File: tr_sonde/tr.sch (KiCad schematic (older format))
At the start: 90 parts, among them J1 SMA, J2 SMA, J3 SMA, K1 SMDHDR, K2 SMDHDR, K3 SMDHDR, Q1 PBSS4250X, Q2 MMBT2222A, Q3 STD2NK90ZT4, Q4 STD2NK90ZT4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

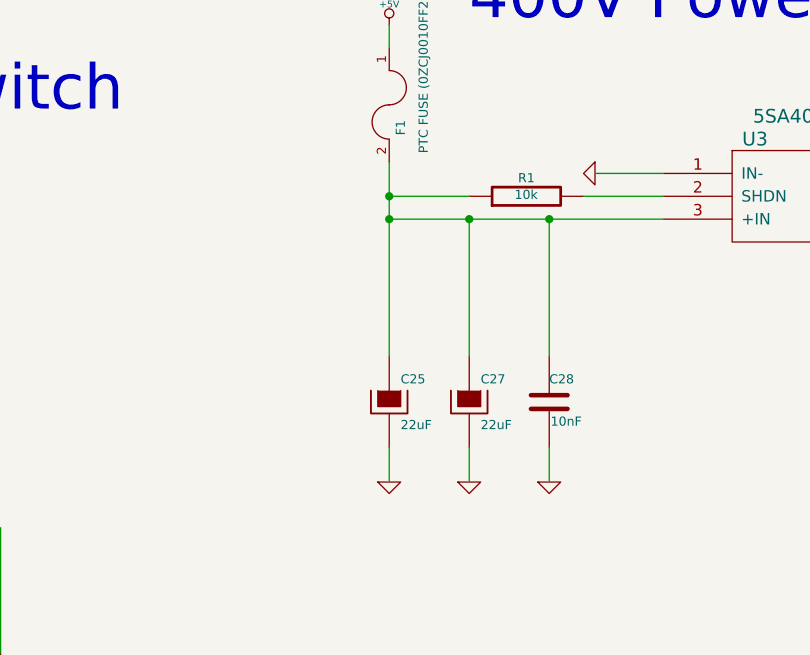
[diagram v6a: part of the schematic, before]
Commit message: component footprint changes to simplify bom
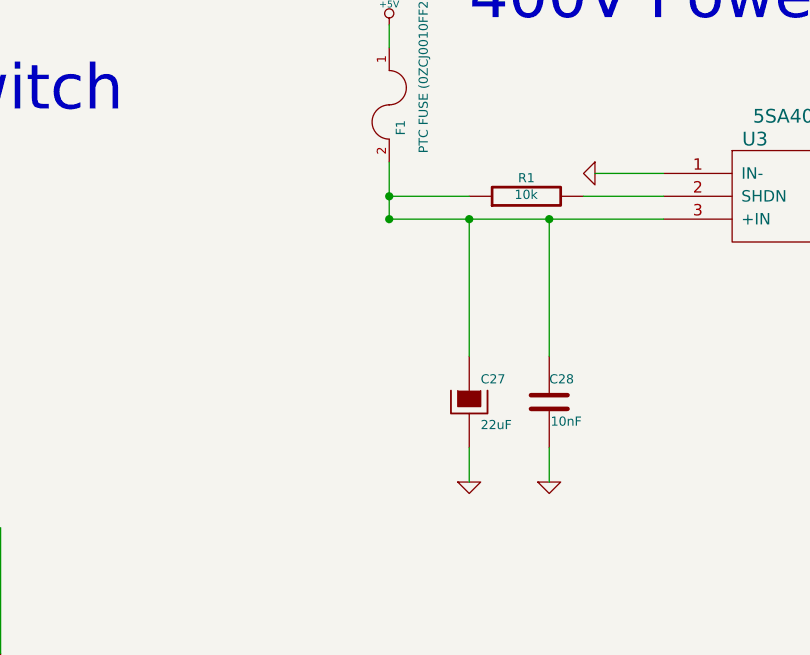
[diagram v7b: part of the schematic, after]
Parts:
- removed C25: 22uF, smd_capacitors:c_1210, symbol CAPAPOL
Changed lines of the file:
@@
-	1    0    0    -1
-$EndComp
-$Comp
-L CAPAPOL C25
-U 1 1 52E6B8A9
-P 8400 2550
-F 0 "C25" H 8450 2650 40  0000 L CNN
-F 1 "22uF" H 8450 2450 40  0000 L CNN
-F 2 "smd_capacitors:c_1210" H 8500 2400 30  0001 C CNN
-F 3 "~" H 8400 2550 300 0000 C CNN
-F 4 "GRM32ER61C476ME15L" H 8400 2550 60  0001 C CNN "DIGIKEYPN"
-	1    8400 2550
-	1    0    0    -1
-$EndComp
-$Comp
-L GND #PWR027
-U 1 1 52E6B8AF
-P 8400 2900
-F 0 "#PWR027" H 8400 2900 30  0001 C CNN
-F 1 "GND" H 8400 2830 30  0001 C CNN
-F 2 "" H 8400 2900 60  0000 C CNN
-F 3 "" H 8400 2900 60  0000 C CNN
-	1    8400 2900
 	1    0    0    -1
 $EndComp
@@
 $EndComp
 $Comp
-L GND #PWR028
+L GND #PWR027
 U 1 1 53376FDF
 P 13900 3550
-F 0 "#PWR028" H 13900 3550 30  0001 C CNN
+F 0 "#PWR027" H 13900 3550 30  0001 C CNN
 F 1 "GND" H 13900 3480 30  0001 C CNN
 F 2 "" H 13900 3550 60  0000 C CNN
@@
 $EndComp
 $Comp
-L VCC #PWR029
+L VCC #PWR028
 U 1 1 5337703B
 P 12750 2900
-F 0 "#PWR029" H 12750 3000 30  0001 C CNN
+F 0 "#PWR028" H 12750 3000 30  0001 C CNN
 F 1 "VCC" H 12750 3000 30  0000 C CNN
 F 2 "" H 12750 2900 60  0000 C CNN
@@
 $EndComp
 $Comp
-L GND #PWR030
+L GND #PWR029
 U 1 1 53484265
 P 11350 2500
-F 0 "#PWR030" H 11350 2500 30  0001 C CNN
+F 0 "#PWR029" H 11350 2500 30  0001 C CNN
 F 1 "GND" H 11350 2430 30  0001 C CNN
 F 2 "" H 11350 2500 60  0000 C CNN
@@
 $EndComp
 $Comp
-L GND #PWR031
+L GND #PWR030
 U 1 1 534843BD
 P 11700 2500
-F 0 "#PWR031" H 11700 2500 30  0001 C CNN
+F 0 "#PWR030" H 11700 2500 30  0001 C CNN
 F 1 "GND" H 11700 2430 30  0001 C CNN
 F 2 "" H 11700 2500 60  0000 C CNN
@@
 $EndComp
 $Comp
-L GND #PWR032
+L GND #PWR031
 U 1 1 534C743A
 P 4950 3400
-F 0 "#PWR032" H 4950 3400 30  0001 C CNN
+F 0 "#PWR031" H 4950 3400 30  0001 C CNN
 F 1 "GND" H 4950 3330 30  0001 C CNN
 F 2 "" H 4950 3400 60  0000 C CNN
@@
 $EndComp
 $Comp
-L +5V #PWR033
+L +5V #PWR032
 U 1 1 537E540A
 P 10900 7350
-F 0 "#PWR033" H 10900 7440 20  0001 C CNN
+F 0 "#PWR032" H 10900 7440 20  0001 C CNN
 F 1 "+5V" H 10900 7440 30  0000 C CNN
 F 2 "" H 10900 7350 60  0000 C CNN
@@
 $EndComp
 $Comp
-L GND #PWR034
+L GND #PWR033
 U 1 1 537E5711
 P 11100 8100
-F 0 "#PWR034" H 11100 8100 30  0001 C CNN
+F 0 "#PWR033" H 11100 8100 30  0001 C CNN
 F 1 "GND" H 11100 8030 30  0001 C CNN
 F 2 "" H 11100 8100 60  0000 C CNN
@@
 $EndComp
 $Comp
-L GND #PWR035
+L GND #PWR034
 U 1 1 537E5906
 P 9700 8650
-F 0 "#PWR035" H 9700 8650 30  0001 C CNN
+F 0 "#PWR034" H 9700 8650 30  0001 C CNN
 F 1 "GND" H 9700 8580 30  0001 C CNN
 F 2 "" H 9700 8650 60  0000 C CNN
@@
 $EndComp
 $Comp
-L +5V #PWR036
+L +5V #PWR035
 U 1 1 537E5D07
 P 15700 5400
-F 0 "#PWR036" H 15700 5490 20  0001 C CNN
+F 0 "#PWR035" H 15700 5490 20  0001 C CNN
 F 1 "+5V" H 15700 5490 30  0000 C CNN
 F 2 "" H 15700 5400 60  0000 C CNN
@@
 $EndComp
 $Comp
-L GND #PWR037
+L GND #PWR036
 U 1 1 537E7018
 P 12400 5600
-F 0 "#PWR037" H 12400 5600 30  0001 C CNN
+F 0 "#PWR036" H 12400 5600 30  0001 C CNN
 F 1 "GND" H 12400 5530 30  0001 C CNN
 F 2 "" H 12400 5600 60  0000 C CNN
@@
 $EndComp
 $Comp
-L GND #PWR038
+L GND #PWR037
 U 1 1 537E737F
 P 12100 5600
-F 0 "#PWR038" H 12100 5600 30  0001 C CNN
+F 0 "#PWR037" H 12100 5600 30  0001 C CNN
 F 1 "GND" H 12100 5530 30  0001 C CNN
 F 2 "" H 12100 5600 60  0000 C CNN
@@
 $EndComp
 $Comp
-L GND #PWR039
+L GND #PWR038
 U 1 1 537E74F6
 P 9300 1550
-F 0 "#PWR039" H 9300 1550 30  0001 C CNN
+F 0 "#PWR038" H 9300 1550 30  0001 C CNN
 F 1 "GND" H 9300 1480 30  0001 C CNN
 F 2 "" H 9300 1550 60  0000 C CNN
@@
 $EndComp
 $Comp
-L GND #PWR040
+L GND #PWR039
 U 1 1 537E78FB
 P 9100 2900
-F 0 "#PWR040" H 9100 2900 30  0001 C CNN
+F 0 "#PWR039" H 9100 2900 30  0001 C CNN
 F 1 "GND" H 9100 2830 30  0001 C CNN
 F 2 "" H 9100 2900 60  0000 C CNN
@@
 $EndComp
 $Comp
-L GND #PWR041
+L GND #PWR040
 U 1 1 537E7FEF
 P 10950 1550
-F 0 "#PWR041" H 10950 1550 30  0001 C CNN
+F 0 "#PWR040" H 10950 1550 30  0001 C CNN
 F 1 "GND" H 10950 1480 30  0001 C CNN
 F 2 "" H 10950 1550 60  0000 C CNN
@@
 $EndComp
 $Comp
-L GND #PWR042
+L GND #PWR041
 U 1 1 537E9221
 P 13500 2550
-F 0 "#PWR042" H 13500 2550 30  0001 C CNN
+F 0 "#PWR041" H 13500 2550 30  0001 C CNN
 F 1 "GND" H 13500 2480 30  0001 C CNN
 F 2 "" H 13500 2550 60  0000 C CNN
@@
 $EndComp
 $Comp
-L VCC #PWR043
+L VCC #PWR042
 U 1 1 537F9103
 P 9200 7600
-F 0 "#PWR043" H 9200 7700 30  0001 C CNN
+F 0 "#PWR042" H 9200 7700 30  0001 C CNN
 F 1 "VCC" H 9200 7700 30  0000 C CNN
 F 2 "" H 9200 7600 60  0000 C CNN
@@
 $EndComp
 $Comp
-L VCC #PWR044
+L VCC #PWR043
 U 1 1 537F913B
 P 11200 9450
-F 0 "#PWR044" H 11200 9550 30  0001 C CNN
+F 0 "#PWR043" H 11200 9550 30  0001 C CNN
 F 1 "VCC" H 11200 9550 30  0000 C CNN
 F 2 "" H 11200 9450 60  0000 C CNN
@@
 $EndComp
 $Comp
-L VDD #PWR045
+L VDD #PWR044
 U 1 1 537FA30C
 P 15550 750
-F 0 "#PWR045" H 15550 850 30  0001 C CNN
+F 0 "#PWR044" H 15550 850 30  0001 C CNN
 F 1 "VDD" H 15550 860 30  0000 C CNN
 F 2 "" H 15550 750 60  0000 C CNN
@@
 $EndComp
 $Comp
-L GND #PWR046
+L GND #PWR045
 U 1 1 537FA865
 P 15550 2950
-F 0 "#PWR046" H 15550 2950 30  0001 C CNN
+F 0 "#PWR045" H 15550 2950 30  0001 C CNN
 F 1 "GND" H 15550 2880 30  0001 C CNN
 F 2 "" H 15550 2950 60  0000 C CNN
@@
 $EndComp
 $Comp
-L GND #PWR047
+L GND #PWR046
 U 1 1 537FAD00
 P 15950 2950
-F 0 "#PWR047" H 15950 2950 30  0001 C CNN
+F 0 "#PWR046" H 15950 2950 30  0001 C CNN
 F 1 "GND" H 15950 2880 30  0001 C CNN
 F 2 "" H 15950 2950 60  0000 C CNN
@@
 $EndComp
 $Comp
-L VCC #PWR048
+L VCC #PWR047
 U 1 1 537FAE62
 P 14200 6300
-F 0 "#PWR048" H 14200 6400 30  0001 C CNN
+F 0 "#PWR047" H 14200 6400 30  0001 C CNN
 F 1 "VCC" H 14200 6400 30  0000 C CNN
 F 2 "" H 14200 6300 60  0000 C CNN
@@
 $EndComp
 $Comp
-L GND #PWR049
+L GND #PWR048
 U 1 1 537FB0A2
 P 14200 7800
-F 0 "#PWR049" H 14200 7800 30  0001 C CNN
+F 0 "#PWR048" H 14200 7800 30  0001 C CNN
 F 1 "GND" H 14200 7730 30  0001 C CNN
 F 2 "" H 14200 7800 60  0000 C CNN
@@
 $EndComp
 $Comp
-L GND #PWR050
+L GND #PWR049
 U 1 1 537FB41D
 P 14550 7800
-F 0 "#PWR050" H 14550 7800 30  0001 C CNN
+F 0 "#PWR049" H 14550 7800 30  0001 C CNN
 F 1 "GND" H 14550 7730 30  0001 C CNN
 F 2 "" H 14550 7800 60  0000 C CNN
@@
 $EndComp
 $Comp
-L GND #PWR051
+L GND #PWR050
 U 1 1 537FBBB2
 P 2900 4800
-F 0 "#PWR051" H 2900 4800 30  0001 C CNN
+F 0 "#PWR050" H 2900 4800 30  0001 C CNN
 F 1 "GND" H 2900 4730 30  0001 C CNN
 F 2 "" H 2900 4800 60  0000 C CNN
@@
 $EndComp
 $Comp
-L VCC #PWR052
+L VCC #PWR051
 U 1 1 537FC621
 P 3500 2550
-F 0 "#PWR052" H 3500 2650 30  0001 C CNN
+F 0 "#PWR051" H 3500 2650 30  0001 C CNN
 F 1 "VCC" H 3500 2650 30  0000 C CNN
 F 2 "" H 3500 2550 60  0000 C CNN
@@
 $EndComp
 $Comp
-L GND #PWR053
+L GND #PWR052
 U 1 1 537FC782
 P 3750 4000
-F 0 "#PWR053" H 3750 4000 30  0001 C CNN
+F 0 "#PWR052" H 3750 4000 30  0001 C CNN
 F 1 "GND" H 3750 3930 30  0001 C CNN
 F 2 "" H 3750 4000 60  0000 C CNN
@@
 $EndComp
 $Comp
-L GND #PWR054
+L GND #PWR053
 U 1 1 537FD975
 P 3300 5200
-F 0 "#PWR054" H 3300 5200 30  0001 C CNN
+F 0 "#PWR053" H 3300 5200 30  0001 C CNN
 F 1 "GND" H 3300 5130 30  0001 C CNN
 F 2 "" H 3300 5200 60  0000 C CNN
@@
 $EndComp
 $Comp
-L +5V #PWR055
+L +5V #PWR054
 U 1 1 5384E6DA
 P 8400 900
-F 0 "#PWR055" H 8400 990 20  0001 C CNN
+F 0 "#PWR054" H 8400 990 20  0001 C CNN
 F 1 "+5V" H 8400 990 30  0000 C CNN
 F 2 "" H 8400 900 60  0000 C CNN
@@
 $EndComp
 $Comp
-L +5V #PWR056
+L +5V #PWR055
 U 1 1 5384E820
 P 12750 4650
-F 0 "#PWR056" H 12750 4740 20  0001 C CNN
+F 0 "#PWR055" H 12750 4740 20  0001 C CNN
 F 1 "+5V" H 12750 4740 30  0000 C CNN
 F 2 "" H 12750 4650 60  0000 C CNN
@@
 $EndComp
 $Comp
-L GND #PWR057
+L GND #PWR056
 U 1 1 5384F0F3
 P 12750 5600
-F 0 "#PWR057" H 12750 5600 30  0001 C CNN
+F 0 "#PWR056" H 12750 5600 30  0001 C CNN
 F 1 "GND" H 12750 5530 30  0001 C CNN
 F 2 "" H 12750 5600 60  0000 C CNN
@@
 $EndComp
 $Comp
-L GND #PWR058
+L GND #PWR057
 U 1 1 53D1771A
 P 15300 2950
-F 0 "#PWR058" H 15300 2950 30  0001 C CNN
+F 0 "#PWR057" H 15300 2950 30  0001 C CNN
 F 1 "GND" H 15300 2880 30  0001 C CNN
 F 2 "" H 15300 2950 60  0000 C CNN
@@
 $EndComp
 $Comp
-L GND #PWR059
+L GND #PWR058
 U 1 1 53D17725
 P 15000 2950
-F 0 "#PWR059" H 15000 2950 30  0001 C CNN
+F 0 "#PWR058" H 15000 2950 30  0001 C CNN
 F 1 "GND" H 15000 2880 30  0001 C CNN
 F 2 "" H 15000 2950 60  0000 C CNN
@@
 $EndComp
 $Comp
-L +5V #PWR060
+L +5V #PWR059
 U 1 1 5417206B
 P 15700 4100
-F 0 "#PWR060" H 15700 4190 20  0001 C CNN
+F 0 "#PWR059" H 15700 4190 20  0001 C CNN
 F 1 "+5V" H 15700 4190 30  0000 C CNN
 F 2 "" H 15700 4100 60  0000 C CNN
@@
 $EndComp
 $Comp
-L VCC #PWR061
+L VCC #PWR060
 U 1 1 54172076
 P 15700 4650
-F 0 "#PWR061" H 15700 4750 30  0001 C CNN
+F 0 "#PWR060" H 15700 4750 30  0001 C CNN
 F 1 "VCC" H 15700 4750 30  0000 C CNN
 F 2 "" H 15700 4650 60  0000 C CNN
@@
 Connection ~ 8400 1750
 Wire Wire Line
-	8400 1500 8400 2350
-Wire Wire Line
 	8400 1750 9600 1750
 Wire Wire Line
@@
 Wire Wire Line
 	11350 2200 11350 2500
-Wire Wire Line
-	8400 2750 8400 2900
 Wire Wire Line
 	8750 2750 8750 2900
@@
 	9550 5800 9750 5800
 $Comp
-L GND #PWR062
+L GND #PWR061
 U 1 1 54CA94E8
 P 8900 6550
-F 0 "#PWR062" H 8900 6550 30  0001 C CNN
+F 0 "#PWR061" H 8900 6550 30  0001 C CNN
 F 1 "GND" H 8900 6480 30  0001 C CNN
 F 2 "" H 8900 6550 60  0000 C CNN
@@
 Text Notes 15800 1450 0    60   ~ 0
 HVMON HEADER\n
+Wire Wire Line
+	8400 1500 8400 1750
 $EndSCHEMATC

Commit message: DFM changes after last protoype rev
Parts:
- removed C10: 4700pF 600V, smd_capacitors:c_1210, symbol C
- removed C26: 100nF, smd_capacitors:c_0805, symbol C
- removed C33: 4700pF 600V, SMD_Packages:SMD-1210, symbol C
- added C8: .022uF 600V, SMD_Packages:SMD-1210, symbol C
- added R10, R15, R20, R9: 10k, smd_capacitors:c_0805, symbol R
- added R21, R23: 150, smd_capacitors:c_1210, symbol R
- added R4: 1k, smd_capacitors:c_0805, symbol R
- added R5, R8: 22, smd_capacitors:c_0805, symbol R
- C1, C13: value 100nF -> 10nF
- R16: value 3k3 -> 10k
- R17: value 15k -> 10k
- R25, R30: value 220 -> 150
- R29: value 510 -> 1k
- R6, R7: value 300 (1W) -> 150
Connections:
- net GND: now also C8.2, R15.2, R20.2; no longer R17.2
- net VCC: now also R21.2, R23.2, R4.1, R5.1; no longer R30.1, R6.2, R7.2
- net VDD: now also C8.1
- net at C3.1, K2.1 (P1), R14.1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: now also R10.2, R9.2
- net at C4.1, K2.2 (PM), R16.1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: now also R10.1, R9.1
- net at Q1.3 (B), Q2.3 (C), R29.2: now also R4.2
- new net: R21.1, R6.2
- new net: R23.1, R7.2
- new net: R15.1, R17.2, R20.1
- new net: R30.1, R8.2
- new net: R5.2, R8.1
